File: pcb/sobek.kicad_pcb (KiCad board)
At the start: 2 copper layers, 222.6 x 67.2 mm, 105 parts, among them SW1 SW_Push, U1 ProMicro

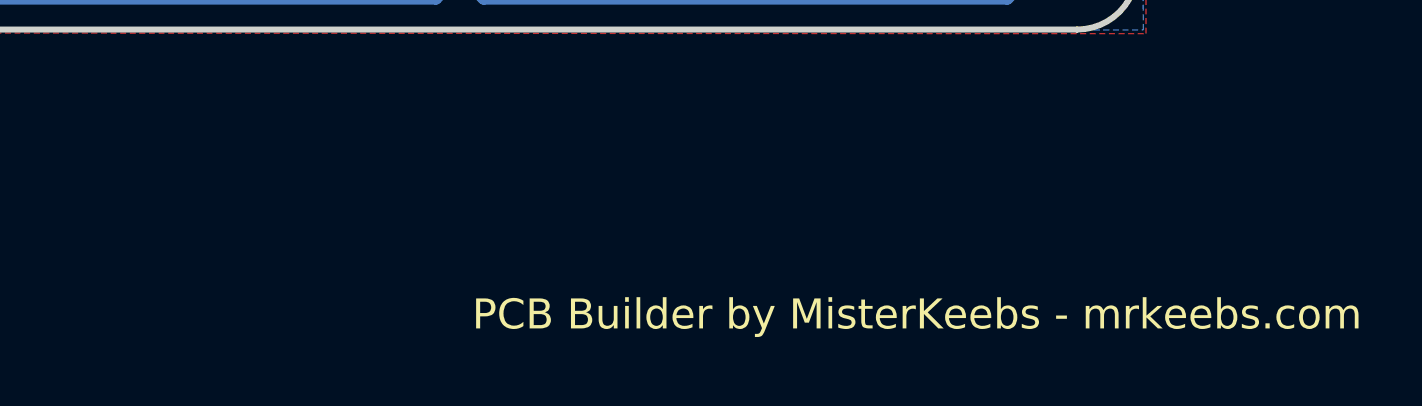
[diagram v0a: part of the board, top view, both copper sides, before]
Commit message: ChangeLog: - remove unnecessary info from board.
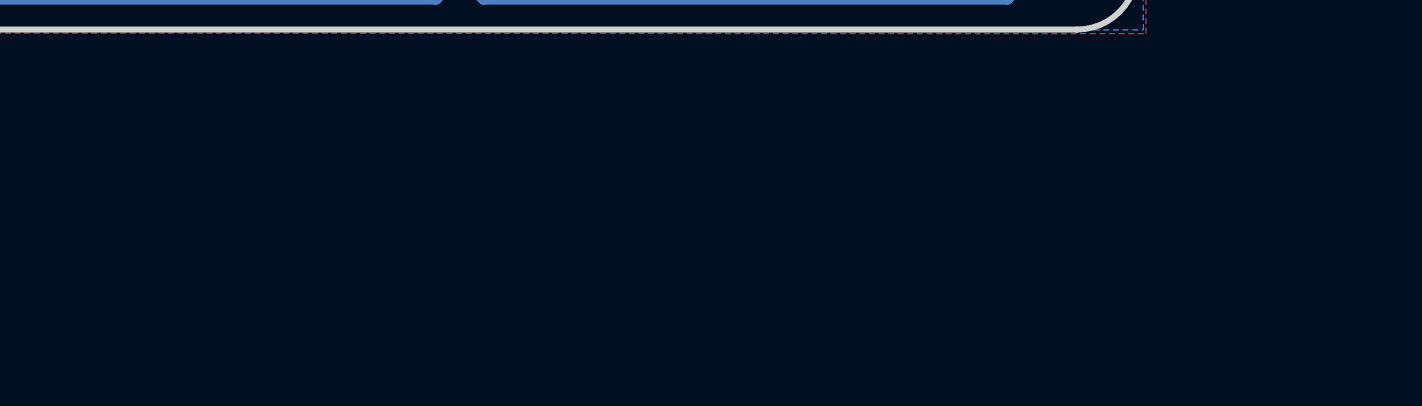
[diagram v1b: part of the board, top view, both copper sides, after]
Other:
- board text removed: "PCB Builder by MisterKeebs - mrkeebs.com"
